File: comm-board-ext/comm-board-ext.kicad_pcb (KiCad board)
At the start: 2 copper layers, 25 x 32 mm, 39 parts, among them J1 GND, J10 MCU-RxD1, J11 MCU-TxD2, J12 MCU-RxD2, J2 GND, J3 +5V, J4 +3.3V, J5 D1-, J6 D1+, J7 D2+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

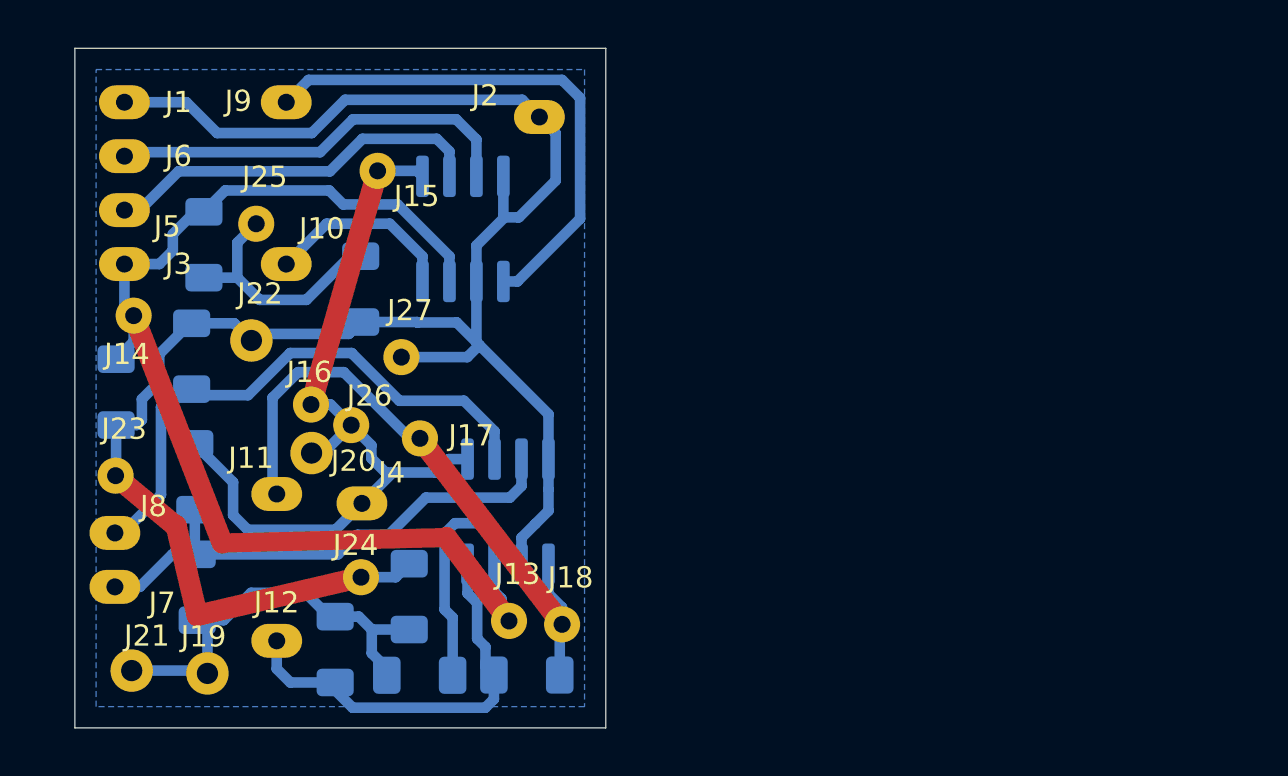
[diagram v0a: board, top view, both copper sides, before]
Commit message: comm-board-ext: Modified for CNC milling
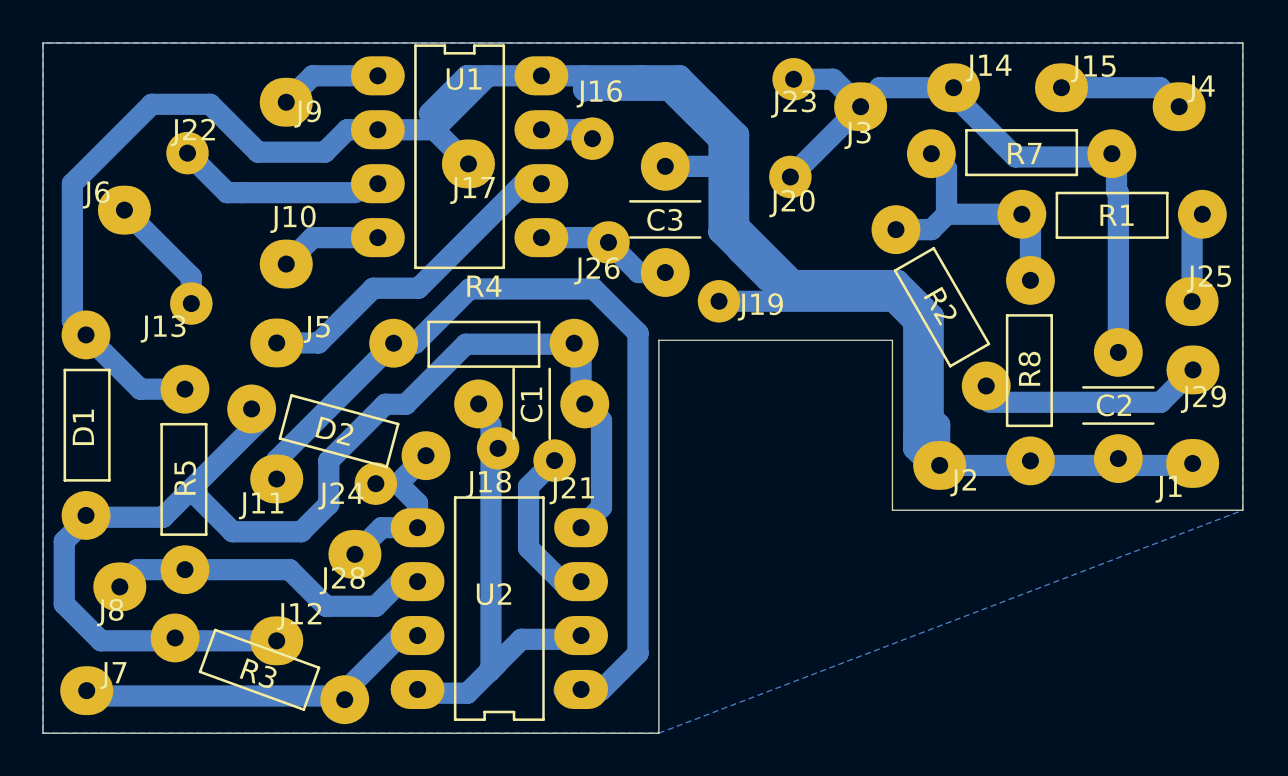
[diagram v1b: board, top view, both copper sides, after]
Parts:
- removed J27: ~, Footprints:VHDR
- removed R6: R, Resistor_SMD:R_1206_3216Metric_Pad1.30x1.75mm_HandSolder
- added C3: C, Footprints:CNC-mill-0.7-CAP, F.Cu at (144.3, 78.3)
- added D1: D, Footprints:CNC-mill-0.7-RES, F.Cu at (117.0, 88.0)
- added D2: D, Footprints:CNC-mill-0.7-RES, F.Cu at (128.9, 88.3)
- added J28: Board - 3.3V, Footprints:CHDR, F.Cu at (129.7, 94.1)
- added J29: MID2 - Board, Footprints:CHDR, F.Cu at (169.2, 85.4)
- C1, C2: footprint Resistor_SMD:R_1206_3216Metric_Pad1.30x1.75mm_HandSolder -> Footprints:CNC-mill-0.7-CAP; moved to F.Cu
- J1, J2: value GND -> GND - DC-DC; footprint Footprints:BBHDR -> Footprints:CHDR
- J10, J11, J12, J5, J6, J7, J8, J9: footprint Footprints:BBHDR -> Footprints:CHDR
- J14: value ~ -> Board - 5V; footprint Footprints:VHDR -> Footprints:CHDR
- J15: value ~ -> Board - 12V; footprint Footprints:VHDR -> Footprints:CHDR
- J17: value ~ -> Board - GND; footprint Footprints:VHDR -> Footprints:CHDR
- J19, J20, J21, J22: footprint Footprints:CHDR -> Footprints:VHDR
- J25: value ~ -> MID1 - Board; footprint Footprints:VHDR -> Footprints:CHDR
- J3: value +5V -> +5V - DC-DC; footprint Footprints:BBHDR -> Footprints:CHDR
- J4: value +3.3V -> +12V - DC-DC; footprint Footprints:BBHDR -> Footprints:CHDR
- R1, R2, R3, R4, R7, R8: footprint Resistor_SMD:R_1206_3216Metric_Pad1.30x1.75mm_HandSolder -> Footprints:CNC-mill-0.7-RES; moved to F.Cu
- R5: value R -> 0; footprint Resistor_SMD:R_1206_3216Metric_Pad1.30x1.75mm_HandSolder -> Footprints:CNC-mill-0.7-RES; moved to F.Cu
- U1, U2: footprint Package_SO:SOIC-8_3.9x4.9mm_P1.27mm -> Footprints:CNC-mill-0.7-DIP-8; moved to F.Cu
- moved J1 53.1 mm to (169.1, 89.8)
- moved C2 47.2 mm to (165.6, 87.1), turned to 180 degrees
- moved R1 44.9 mm to (165.3, 78.1)
- moved J25 44.2 mm to (169.1, 82.2)
- moved J4 42.8 mm to (168.5, 73.0)
- moved J14 40.1 mm to (157.9, 72.1)
- moved R7 38.7 mm to (161.1, 75.2), turned to 90 degrees
- moved J23 37.0 mm to (150.3, 71.7)
- moved J3 35.4 mm to (153.5, 73.0)
- moved R2 32.8 mm to (157.3, 82.5), turned to 30 degrees
- moved J15 32.4 mm to (163.0, 72.1)
- moved R8 31.8 mm to (161.5, 85.4), turned to 180 degrees
- moved J19 29.8 mm to (146.8, 82.2)
- moved J20 26.0 mm to (150.2, 76.3)
- moved J2 25.0 mm to (157.2, 89.9)
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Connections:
- C1 pad 1: Net-(J19-Pin_1) -> /RxD2
- J13 pad 1: +5V -> /Dp1
- J15 pad 1: +3.3V -> +12V
- J16 pad 1: +3.3V -> /Dp1
- J17 pad 1: /TxD2 -> GND
- J18 pad 1: /TxD2 -> GND
- J19 pad 1: Net-(J19-Pin_1) -> GND
- J20 pad 1: +3.3V -> +5V
- J21 pad 1: Net-(J19-Pin_1) -> +5V
- J22 pad 1: GND -> +5V
- J23 pad 1: GND -> +5V
- J24 pad 1: GND -> +3.3V
- J4 pad 1: +3.3V -> +12V
- R1 pad 1: +3.3V -> Net-(R1-Pad1)
- R1 pad 2: /Dp2 -> Net-(J25-Pin_1)
- R2 pad 1: /RxD2 -> Net-(J29-Pin_1)
- R2 pad 2: Net-(J19-Pin_1) -> Net-(R1-Pad1)
- R3 pad 1: Net-(J19-Pin_1) -> /RxD2
- R7 pad 2: Net-(J25-Pin_1) -> Net-(R1-Pad1)
- R8 pad 1: GND -> Net-(R1-Pad1)
- R8 pad 2: Net-(J25-Pin_1) -> GND
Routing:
- net GND: track 78.8 -> 153.2 mm
- net /RxD2: track 20.1 -> 58.7 mm
- net /TxD2: track 18.9 -> 41.4 mm
- net Net-(J19-Pin_1): track 20.0 -> 0.00 mm
- net /TxD1: track 25.1 -> 5.99 mm
- net Net-(R1-Pad1): track 0.00 -> 11.8 mm
- net +3.3V: track 27.0 -> 15.3 mm
- net /Dp1: track 19.9 -> 8.46 mm
- net /Dm2: track 26.7 -> 15.5 mm
- net Net-(J29-Pin_1): track 0.00 -> 10.2 mm
- net +5V: track 38.0 -> 48.0 mm
- net /Dp2: track 24.7 -> 16.3 mm
- net Net-(J25-Pin_1): track 11.6 -> 4.31 mm
- net +12V: track 0.00 -> 5.91 mm
- net /RxD1: track 9.02 -> 4.83 mm
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- added copper zone on B.Cu, net (none)
- removed copper zone on B.Cu, net GND
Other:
- board size 25 x 32 mm -> 56.5 x 32.5 mm
- copper layers 2 -> 4
- board text removed: "RPi - 5V"
- board text removed: "RPi - GND"
- board text removed: "RPi - RxD"
- board text removed: "RPi - TxD"
- board text removed: "RPi - cable holder"
- board text removed: "RPi - connect"
